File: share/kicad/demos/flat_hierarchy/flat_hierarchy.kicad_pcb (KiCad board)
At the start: 2 copper layers, 160 x 99.1 mm, 64 parts, among them J1 DB9-FEMAL, P1 CONN_2, P2 SUPP28, P3 SUPP40, Q1 BC237, Q2 BC307, Q3 BC307, U1 24Cxx, U2 74HC125, U3 7805, U4 LT1373, U5 PIC_18_PINS, U6 PIC_8_PINS

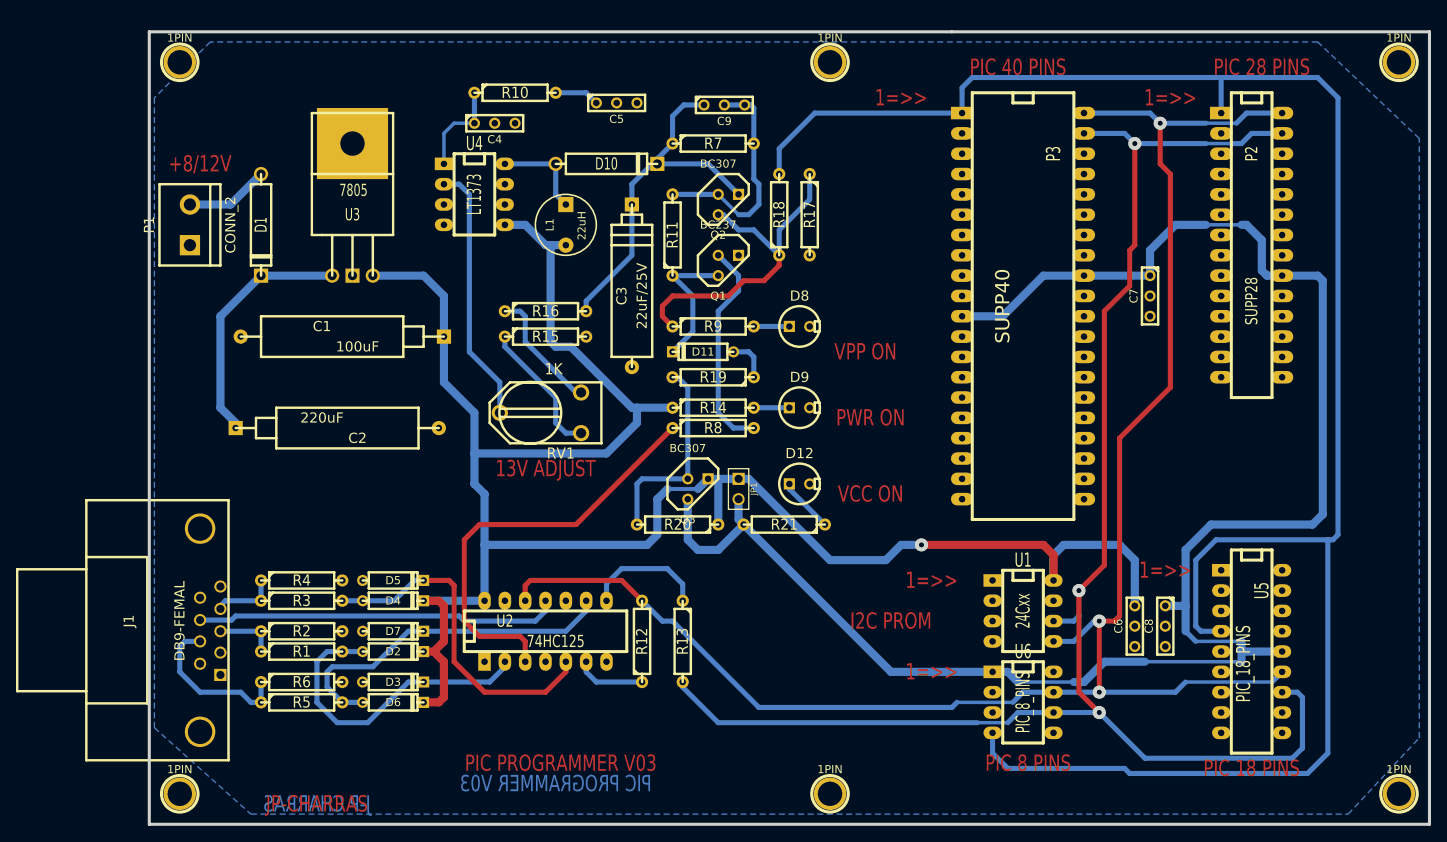
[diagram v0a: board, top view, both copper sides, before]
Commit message: Remove KiCad V4.0.7
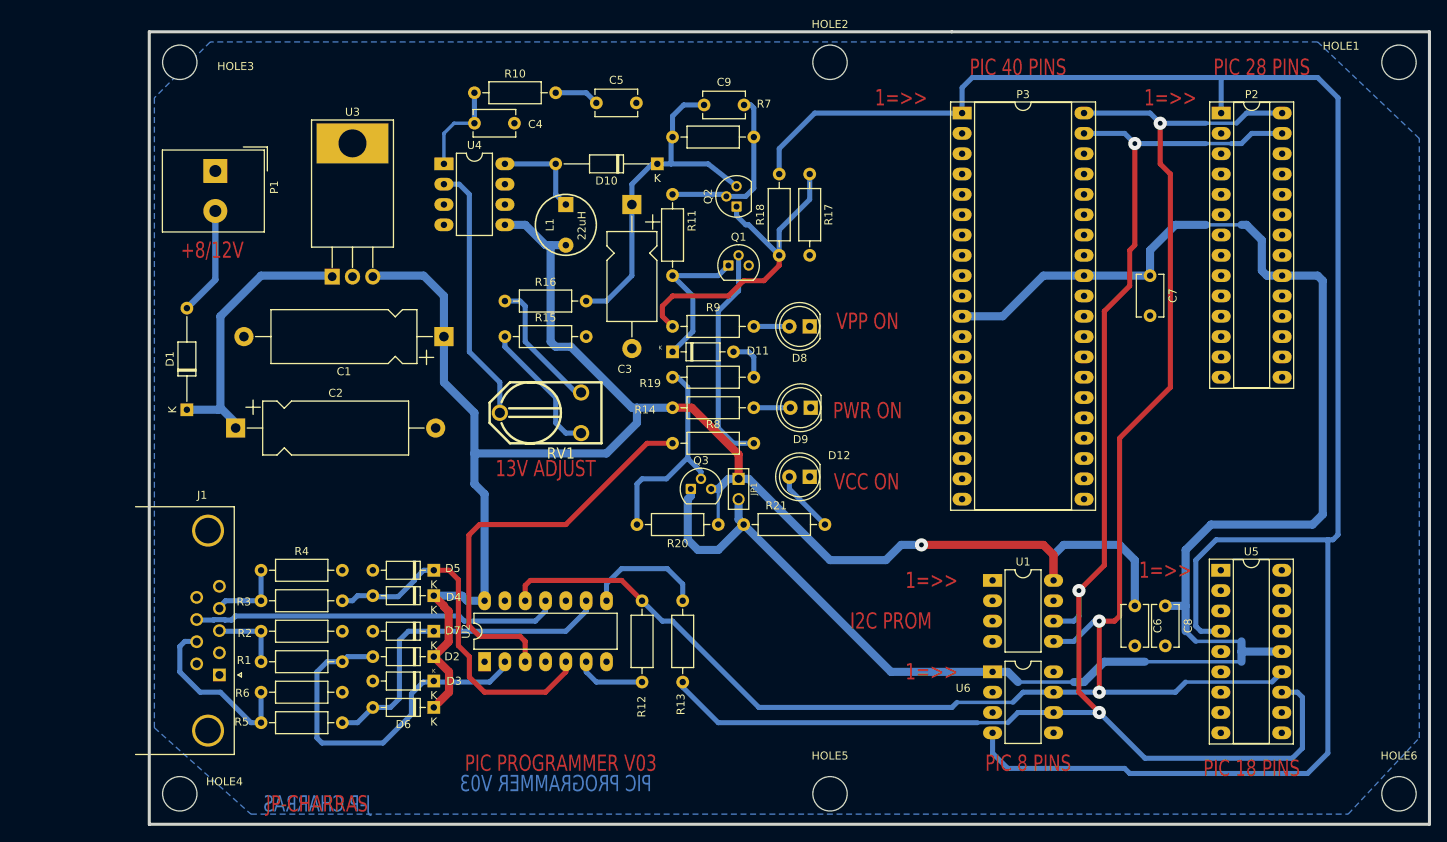
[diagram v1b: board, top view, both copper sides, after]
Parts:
- C1, C2: footprint discret:CP10 -> Capacitor_THT:CP_Axial_L18.0mm_D6.5mm_P25.00mm_Horizontal
- C3: footprint discret:CP8 -> Capacitor_THT:CP_Axial_L11.0mm_D6.0mm_P18.00mm_Horizontal
- C4, C5, C6, C7, C8, C9: footprint discret:C1-1 -> Capacitor_THT:C_Disc_D5.1mm_W3.2mm_P5.00mm
- D1, D10: footprint discret:D5 -> Diode_THT:D_DO-35_SOD27_P12.70mm_Horizontal
- D11, D2, D3, D4, D5, D6, D7: footprint discret:D3 -> Diode_THT:D_DO-35_SOD27_P7.62mm_Horizontal
- D12, D8, D9: footprint discret:LEDV -> LED_THT:LED_D5.0mm
- HOLE1, HOLE2, HOLE3, HOLE4, HOLE5, HOLE6: renamed from 1PIN; footprint 1pin -> MountingHole:MountingHole_4.3mm_M4_DIN965
- J1: footprint connect:DB9FC -> Connector_Dsub:DSUB-9_Female_Horizontal_P2.77x2.84mm_EdgePinOffset7.70mm_Housed_MountingHolesOffset9.12mm
- P1: footprint connect:bornier2 -> TerminalBlock_Altech:Altech_AK300_1x02_P5.00mm_45-Degree
- P2: footprint 28DIP-ELL300 -> Package_DIP:DIP-28_W7.62mm_Socket_LongPads
- P3: footprint 40DIP-ELL600 -> Package_DIP:DIP-40_W15.24mm_Socket_LongPads
- Q1, Q2, Q3: footprint discret:TO92 -> Package_TO_SOT_THT:TO-92
- R1, R11, R12, R13, R14, R15, R16, R17, R18, R19, R2, R20, R21, R3, R4, R5, R6, R7, R8, R9: footprint discret:R4 -> Resistor_THT:R_Axial_DIN0207_L6.3mm_D2.5mm_P10.16mm_Horizontal
- R10: value 5,1K -> 5.1K; footprint discret:R4 -> Resistor_THT:R_Axial_DIN0207_L6.3mm_D2.5mm_P10.16mm_Horizontal
- RV1: footprint discret:RV2X4 -> pic_programmer_fp:RV2X4
- U1, U4, U6: footprint dip_sockets:DIP-8__300_ELL -> Package_DIP:DIP-8_W7.62mm_LongPads
- U2: footprint dip_sockets:DIP-14__300_ELL -> Package_DIP:DIP-14_W7.62mm_LongPads
- U3: footprint discret:LM78XX -> Package_TO_SOT_THT:TO-220-3_Horizontal_TabDown
- U5: footprint dip_sockets:DIP-18__300_ELL -> Package_DIP:DIP-18_W7.62mm_Socket_LongPads
- moved P3 25.3 mm to (175.3, 50.8), turned to 0 degrees
- moved D1 24.9 mm to (78.4, 87.9), turned to 90 degrees
- moved P2 16.9 mm to (207.6, 50.8), turned to 0 degrees
- moved C2 12.7 mm to (84.5, 90.2)
- moved C1 12.7 mm to (110.5, 78.7)
- moved U5 10.9 mm to (207.6, 108.0), turned to 0 degrees
- moved C3 10.2 mm to (134.0, 62.2)
- moved U2 8.52 mm to (115.6, 119.4), turned to 90 degrees
- moved P1 7.44 mm to (81.9, 58.0), turned to -90 degrees
- moved D10 6.35 mm to (137.2, 57.1), turned to 180 degrees
- moved R5 5.68 mm to (87.6, 127.0)
- moved RV1 5.68 mm to (127.6, 90.8)
- moved J1 5.58 mm to (82.4, 121.0), turned to -90 degrees
- moved R8 5.43 mm to (139.1, 92.1)
- moved U1 5.39 mm to (179.1, 109.2), turned to 0 degrees
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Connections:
- net /pic_programmer/CTS renamed /pic_programmer/PC-DATA-IN
- net /pic_programmer/DTR renamed /pic_programmer/PC-DATA-OUT
- net /pic_programmer/TXD renamed /pic_programmer/VPP_ON
- D1 pad 1: Net-(D1-Pad1) -> Net-(C2-Pad1)
- D1 pad 2: Net-(C2-Pad1) -> Net-(D1-Pad2)
- D10 pad 1: Net-(D10-Pad1) -> VPP
- D10 pad 2: VPP -> Net-(D10-Pad2)
- D12 pad 1: Net-(D12-Pad1) -> GND
- D12 pad 2: GND -> Net-(D12-Pad2)
- D2 pad 1: Net-(D2-Pad1) -> VCC
- D2 pad 2: VCC -> Net-(D2-Pad2)
- D3 pad 1: GND -> Net-(D2-Pad2)
- D3 pad 2: Net-(D2-Pad1) -> GND
- D4 pad 1: Net-(D4-Pad1) -> VCC
- D4 pad 2: VCC -> Net-(D4-Pad2)
- D5 pad 1: GND -> Net-(D4-Pad2)
- D5 pad 2: Net-(D4-Pad1) -> GND
- D6 pad 1: Net-(D6-Pad1) -> VCC
- D6 pad 2: VCC -> Net-(D6-Pad2)
- D7 pad 1: GND -> Net-(D6-Pad2)
- D7 pad 2: Net-(D6-Pad1) -> GND
- D8 pad 1: Net-(D8-Pad1) -> GND
- D8 pad 2: GND -> Net-(D8-Pad2)
- D9 pad 1: Net-(D9-Pad1) -> GND
- D9 pad 2: GND -> Net-(D9-Pad2)
- J1 pad 1: (no net) -> unconnected-(J1-Pad1)
- J1 pad 2: (no net) -> unconnected-(J1-Pad2)
- J1 pad 6: (no net) -> unconnected-(J1-Pad6)
- J1 pad 9: (no net) -> unconnected-(J1-Pad9)
- L1 pad 1: Net-(D10-Pad1) -> Net-(D10-Pad2)
- P1 pad 2: Net-(D1-Pad1) -> Net-(D1-Pad2)
- P2 pad 10: (no net) -> unconnected-(P2-Pad10)
- P2 pad 11: (no net) -> unconnected-(P2-Pad11)
- P2 pad 12: (no net) -> unconnected-(P2-Pad12)
- P2 pad 13: (no net) -> unconnected-(P2-Pad13)
- P2 pad 14: (no net) -> unconnected-(P2-Pad14)
- P2 pad 15: (no net) -> unconnected-(P2-Pad15)
- P2 pad 16: (no net) -> unconnected-(P2-Pad16)
- P2 pad 17: (no net) -> unconnected-(P2-Pad17)
- P2 pad 18: (no net) -> unconnected-(P2-Pad18)
- P2 pad 2: (no net) -> unconnected-(P2-Pad2)
- P2 pad 21: (no net) -> unconnected-(P2-Pad21)
- P2 pad 22: (no net) -> unconnected-(P2-Pad22)
- P2 pad 23: (no net) -> unconnected-(P2-Pad23)
- P2 pad 24: (no net) -> unconnected-(P2-Pad24)
- P2 pad 25: (no net) -> unconnected-(P2-Pad25)
- P2 pad 26: (no net) -> unconnected-(P2-Pad26)
- P2 pad 3: (no net) -> unconnected-(P2-Pad3)
- P2 pad 4: (no net) -> unconnected-(P2-Pad4)
- P2 pad 5: (no net) -> unconnected-(P2-Pad5)
- P2 pad 6: (no net) -> unconnected-(P2-Pad6)
- P2 pad 7: (no net) -> unconnected-(P2-Pad7)
- P2 pad 9: (no net) -> unconnected-(P2-Pad9)
- P3 pad 10: (no net) -> unconnected-(P3-Pad10)
- P3 pad 13: (no net) -> unconnected-(P3-Pad13)
- P3 pad 14: (no net) -> unconnected-(P3-Pad14)
- P3 pad 15: (no net) -> unconnected-(P3-Pad15)
- P3 pad 16: (no net) -> unconnected-(P3-Pad16)
- P3 pad 17: (no net) -> unconnected-(P3-Pad17)
- P3 pad 18: (no net) -> unconnected-(P3-Pad18)
- P3 pad 19: (no net) -> unconnected-(P3-Pad19)
- P3 pad 2: (no net) -> unconnected-(P3-Pad2)
- P3 pad 20: (no net) -> unconnected-(P3-Pad20)
- P3 pad 21: (no net) -> unconnected-(P3-Pad21)
- P3 pad 22: (no net) -> unconnected-(P3-Pad22)
- P3 pad 23: (no net) -> unconnected-(P3-Pad23)
- P3 pad 24: (no net) -> unconnected-(P3-Pad24)
- P3 pad 25: (no net) -> unconnected-(P3-Pad25)
- P3 pad 26: (no net) -> unconnected-(P3-Pad26)
- P3 pad 27: (no net) -> unconnected-(P3-Pad27)
- P3 pad 28: (no net) -> unconnected-(P3-Pad28)
- P3 pad 29: (no net) -> unconnected-(P3-Pad29)
- P3 pad 3: (no net) -> unconnected-(P3-Pad3)
- P3 pad 30: (no net) -> unconnected-(P3-Pad30)
- P3 pad 33: (no net) -> unconnected-(P3-Pad33)
- P3 pad 34: (no net) -> unconnected-(P3-Pad34)
- P3 pad 35: (no net) -> unconnected-(P3-Pad35)
- P3 pad 36: (no net) -> unconnected-(P3-Pad36)
- P3 pad 37: (no net) -> unconnected-(P3-Pad37)
- P3 pad 38: (no net) -> unconnected-(P3-Pad38)
- P3 pad 4: (no net) -> unconnected-(P3-Pad4)
- P3 pad 5: (no net) -> unconnected-(P3-Pad5)
- P3 pad 6: (no net) -> unconnected-(P3-Pad6)
- P3 pad 7: (no net) -> unconnected-(P3-Pad7)
- P3 pad 9: (no net) -> unconnected-(P3-Pad9)
- Q1 pad 1: GND -> Net-(D11-Pad1)
- Q1 pad 3: Net-(D11-Pad2) -> GND
- Q2 pad 1: VPP -> Net-(Q2-Pad1)
- Q2 pad 3: Net-(Q2-Pad3) -> VPP
- Q3 pad 1: VCC -> VCC_PIC
- Q3 pad 3: VCC_PIC -> VCC
- R1 pad 2: Net-(D2-Pad1) -> Net-(D2-Pad2)
- R11 pad 1: Net-(D11-Pad2) -> Net-(D11-Pad1)
- R14 pad 2: Net-(D9-Pad1) -> Net-(D9-Pad2)
- R17 pad 1: Net-(Q2-Pad3) -> Net-(Q2-Pad1)
- R18 pad 1: Net-(Q2-Pad3) -> Net-(Q2-Pad1)
- R19 pad 1: Net-(D11-Pad1) -> Net-(D11-Pad2)
- R21 pad 1: Net-(D12-Pad1) -> VCC_PIC
- R21 pad 2: VCC_PIC -> Net-(D12-Pad2)
- R3 pad 2: Net-(D4-Pad1) -> Net-(D4-Pad2)
- R5 pad 2: Net-(D6-Pad1) -> Net-(D6-Pad2)
- R9 pad 1: Net-(Q2-Pad3) -> Net-(Q2-Pad1)
- R9 pad 2: Net-(D8-Pad1) -> Net-(D8-Pad2)
- U1 pad 7: (no net) -> unconnected-(U1-Pad7)
- U2 pad 2: Net-(D2-Pad1) -> Net-(D2-Pad2)
- U2 pad 5: Net-(D4-Pad1) -> Net-(D4-Pad2)
- U2 pad 9: Net-(D6-Pad1) -> Net-(D6-Pad2)
- U4 pad 3: (no net) -> unconnected-(U4-Pad3)
- U4 pad 4: (no net) -> unconnected-(U4-Pad4)
- U4 pad 8: Net-(D10-Pad1) -> Net-(D10-Pad2)
- U5 pad 1: (no net) -> unconnected-(U5-Pad1)
- U5 pad 10: (no net) -> unconnected-(U5-Pad10)
- U5 pad 11: (no net) -> unconnected-(U5-Pad11)
- U5 pad 15: (no net) -> unconnected-(U5-Pad15)
- U5 pad 16: (no net) -> unconnected-(U5-Pad16)
- U5 pad 17: (no net) -> unconnected-(U5-Pad17)
- U5 pad 18: (no net) -> unconnected-(U5-Pad18)
- U5 pad 2: (no net) -> unconnected-(U5-Pad2)
- U5 pad 3: (no net) -> unconnected-(U5-Pad3)
- U5 pad 6: (no net) -> unconnected-(U5-Pad6)
- U5 pad 7: (no net) -> unconnected-(U5-Pad7)
- U5 pad 8: (no net) -> unconnected-(U5-Pad8)
- U5 pad 9: (no net) -> unconnected-(U5-Pad9)
- U6 pad 2: (no net) -> unconnected-(U6-Pad2)
- U6 pad 3: (no net) -> unconnected-(U6-Pad3)
- U6 pad 5: (no net) -> unconnected-(U6-Pad5)
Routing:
- net Net-(D2-Pad2): track 0.00 -> 45.9 mm
- net Net-(D4-Pad2): track 0.00 -> 44.7 mm
- net Net-(D6-Pad1): track 44.0 -> 0.00 mm
- net Net-(D4-Pad1): track 42.7 -> 0.00 mm
- net Net-(Q2-Pad3): track 42.5 -> 0.00 mm
- net Net-(D6-Pad2): track 0.00 -> 41.8 mm
- net Net-(Q2-Pad1): track 0.00 -> 41.3 mm
- net Net-(D2-Pad1): track 39.4 -> 0.00 mm
- net VCC: track 252.2 -> 226.7 mm
- net Net-(D11-Pad1): track 5.34 -> 19.1 mm
- net Net-(D1-Pad2): track 0.00 -> 13.6 mm
- net Net-(D11-Pad2): track 17.3 -> 5.34 mm
- net Net-(D10-Pad2): track 0.00 -> 12.0 mm
- net Net-(D10-Pad1): track 12.0 -> 0.00 mm
- net Net-(D1-Pad1): track 10.5 -> 0.00 mm
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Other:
- net class Default removed
- rule pad_to_mask_clearance: 0.2 -> 0
